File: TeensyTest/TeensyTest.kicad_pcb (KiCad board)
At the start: 2 copper layers, 45 x 34 mm, 31 parts, among them J2 Conn_01x08_Female, J3 Conn_01x03_Female, P1 USB_C_Plug_USB2.0, SW1 SW_Push, SW2 SW_Push, U1 AP2114H, U2 MK20DX256VLH7, U3 MKL02Z32VFG4, Y1 Crystal_GND24

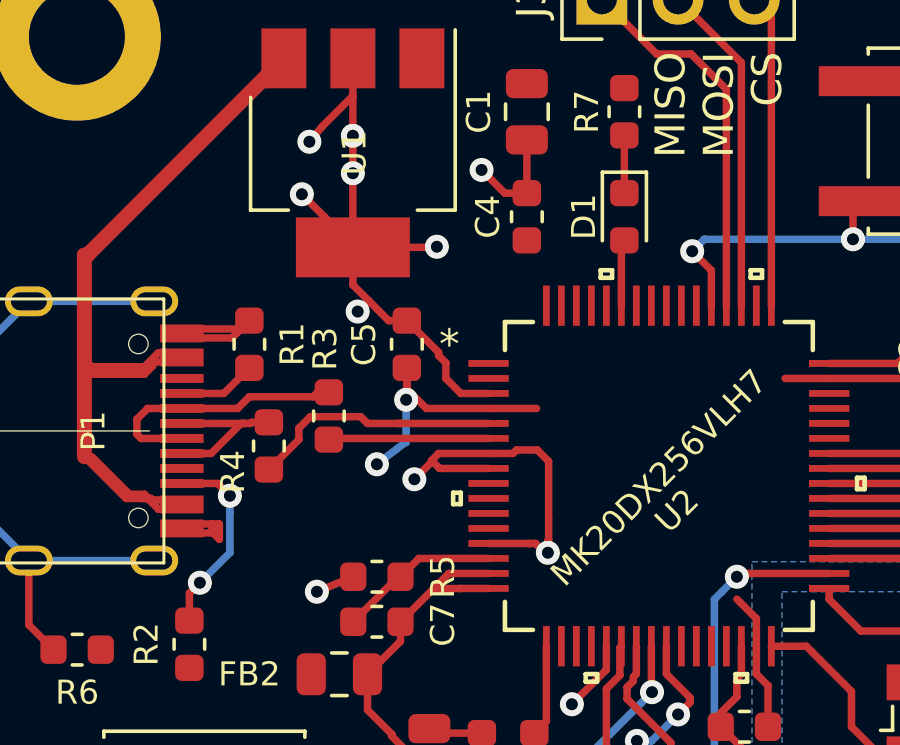
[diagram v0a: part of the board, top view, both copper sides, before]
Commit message: Moved C4 closer to pins 7 & 8
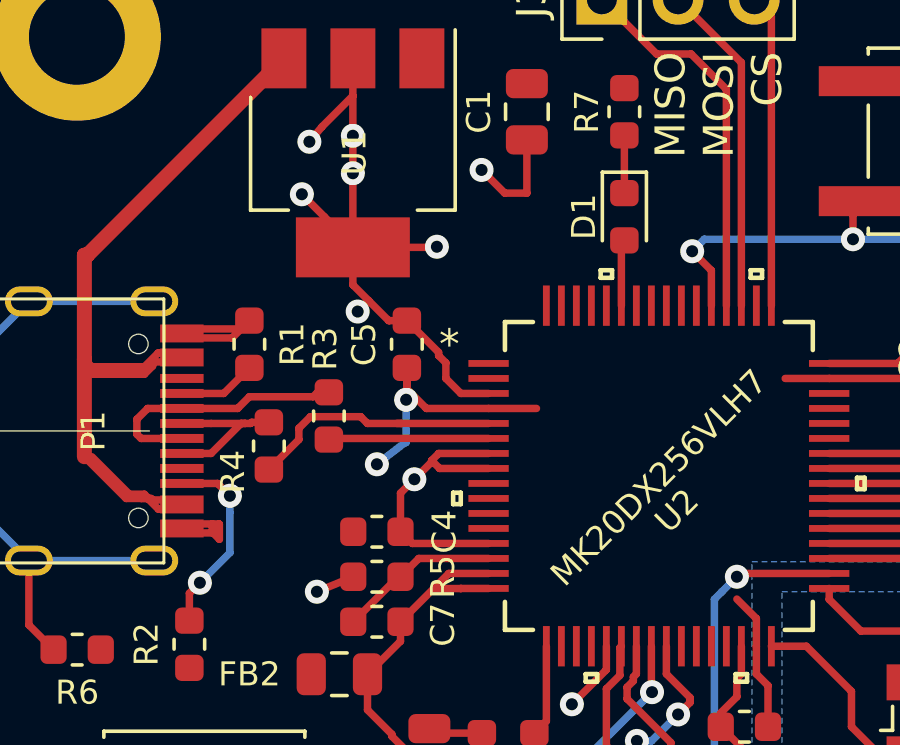
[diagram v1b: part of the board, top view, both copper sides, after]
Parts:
- moved C4 11.6 mm to (29.1, 55.9), turned to 0 degrees
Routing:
- net +3V3: track 61.7 -> 59.4 mm, vias 15 -> 14
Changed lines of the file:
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@@
     (thickness 1.6)
     (drawings 12)
-    (tracks 359)
+    (tracks 349)
     (zones 0)
     (modules 31)
@@
   )
   (module Capacitor_SMD:C_0603_1608Metric (layer F.Cu)
-    (at 34.1 45.36 90)
+    (at 29.1 55.86)
     (descr "Capacitor SMD 0603 (1608 Metric), square (rectangular) end terminal, IPC_7351 nominal, (Body size source: http://www.tortai-tech.com/upload/download/2011102023233369053.pdf), generated with kicad-footprint-generator")
     (tags capacitor)
     (attr smd)
-    (fp_text reference C4 (at 0 -1.3 90) (layer F.SilkS)
-      (effects (font (size 0.8 0.8) (thickness 0.1)))
-    )
-    (fp_text value 0.1uF (at 0 1.43 90) (layer F.Fab)
-      (effects (font (size 0.8 0.8) (thickness 0.1)))
-    )
-    (fp_text user %R (at 0 0 90) (layer F.Fab)
+    (fp_text reference C4 (at 2.25 0 90) (layer F.SilkS)
+      (effects (font (size 0.8 0.8) (thickness 0.1)))
+    )
+    (fp_text value 0.1uF (at 0 1.43) (layer F.Fab)
+      (effects (font (size 0.8 0.8) (thickness 0.1)))
+    )
+    (fp_text user %R (at 0 0) (layer F.Fab)
       (effects (font (size 0.8 0.8) (thickness 0.1)))
     )
@@
     (fp_line (start -0.8 -0.4) (end 0.8 -0.4) (layer F.Fab) (width 0.1))
     (fp_line (start -0.8 0.4) (end -0.8 -0.4) (layer F.Fab) (width 0.1))
-    (pad 2 smd roundrect (at 0.7875 0 90) (size 0.875 0.95) (layers F.Cu F.Paste F.Mask) (roundrect_rratio 0.25)
+    (pad 2 smd roundrect (at 0.7875 0) (size 0.875 0.95) (layers F.Cu F.Paste F.Mask) (roundrect_rratio 0.25)
       (net 1 +3V3))
-    (pad 1 smd roundrect (at -0.7875 0 90) (size 0.875 0.95) (layers F.Cu F.Paste F.Mask) (roundrect_rratio 0.25)
+    (pad 1 smd roundrect (at -0.7875 0) (size 0.875 0.95) (layers F.Cu F.Paste F.Mask) (roundrect_rratio 0.25)
       (net 2 GND))
     (model ${KISYS3DMOD}/Capacitor_SMD.3dshapes/C_0603_1608Metric.wrl
@@
   (segment (start 41.705684 67.139999) (end 41.705684 68.184316) (width 0.25) (layer B.Cu) (net 1))
   (segment (start 41.705684 68.184316) (end 41.22 68.67) (width 0.25) (layer B.Cu) (net 1))
-  (segment (start 33.636984 53.249999) (end 33.751998 53.134985) (width 0.25) (layer F.Cu) (net 1))
-  (segment (start 34.448002 53.134985) (end 34.825002 53.511985) (width 0.25) (layer F.Cu) (net 1))
-  (segment (start 34.825002 53.511985) (end 34.825002 55.458002) (width 0.25) (layer F.Cu) (net 1))
-  (segment (start 33.751998 53.134985) (end 34.448002 53.134985) (width 0.25) (layer F.Cu) (net 1))
-  (segment (start 32.8231 53.249999) (end 33.636984 53.249999) (width 0.25) (layer F.Cu) (net 1))
   (segment (start 28.3125 57.36) (end 27.1 57.86) (width 0.25) (layer F.Cu) (net 1))
   (via (at 27.1 57.86) (size 0.8) (drill 0.4) (layers F.Cu B.Cu) (net 1))
-  (via (at 34.8 56.56) (size 0.8) (drill 0.4) (layers F.Cu B.Cu) (net 1))
-  (segment (start 34.825002 55.458002) (end 34.825002 56.134998) (width 0.25) (layer F.Cu) (net 1))
-  (segment (start 34.8 56.16) (end 34.8 56.56) (width 0.25) (layer F.Cu) (net 1))
-  (segment (start 34.825002 56.134998) (end 34.8 56.16) (width 0.25) (layer F.Cu) (net 1))
-  (segment (start 34.190001 56.250001) (end 34.2 56.26) (width 0.25) (layer F.Cu) (net 1))
-  (segment (start 32.8231 56.250001) (end 34.190001 56.250001) (width 0.25) (layer F.Cu) (net 1))
-  (segment (start 34.190001 56.250001) (end 34.390001 56.250001) (width 0.25) (layer F.Cu) (net 1))
-  (segment (start 34.7 56.56) (end 34.8 56.56) (width 0.25) (layer F.Cu) (net 1))
-  (segment (start 34.390001 56.250001) (end 34.7 56.56) (width 0.25) (layer F.Cu) (net 1))
   (segment (start 32.8231 53.75) (end 31.19 53.75) (width 0.25) (layer F.Cu) (net 1))
   (segment (start 31.19 53.75) (end 30.925 53.485) (width 0.25) (layer F.Cu) (net 1))
@@
   (segment (start 30.925 53.535) (end 30.35 54.11) (width 0.25) (layer F.Cu) (net 1))
   (segment (start 30.925 53.485) (end 30.925 53.535) (width 0.25) (layer F.Cu) (net 1))
+  (segment (start 29.8875 54.5725) (end 30.35 54.11) (width 0.25) (layer F.Cu) (net 1))
+  (segment (start 29.8875 55.86) (end 29.8875 54.5725) (width 0.25) (layer F.Cu) (net 1))
+  (segment (start 30.277501 56.250001) (end 29.8875 55.86) (width 0.25) (layer F.Cu) (net 1))
+  (segment (start 32.8231 56.250001) (end 30.277501 56.250001) (width 0.25) (layer F.Cu) (net 1))
   (segment (start 24.5725 49.1) (end 24.85 48.8225) (width 0.25) (layer F.Cu) (net 2))
   (segment (start 22.6 49.1) (end 24.5725 49.1) (width 0.25) (layer F.Cu) (net 2))

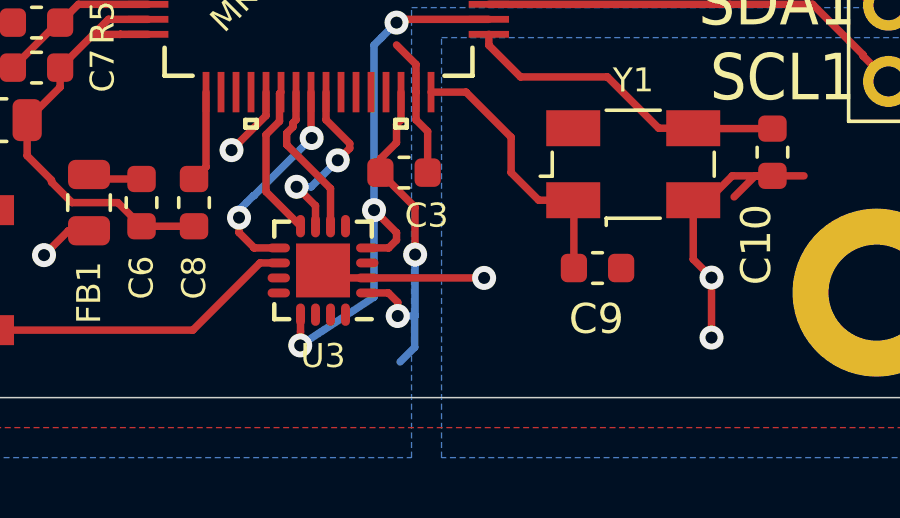
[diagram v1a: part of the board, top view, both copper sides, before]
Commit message: Added extra 100nF cap for MKL02
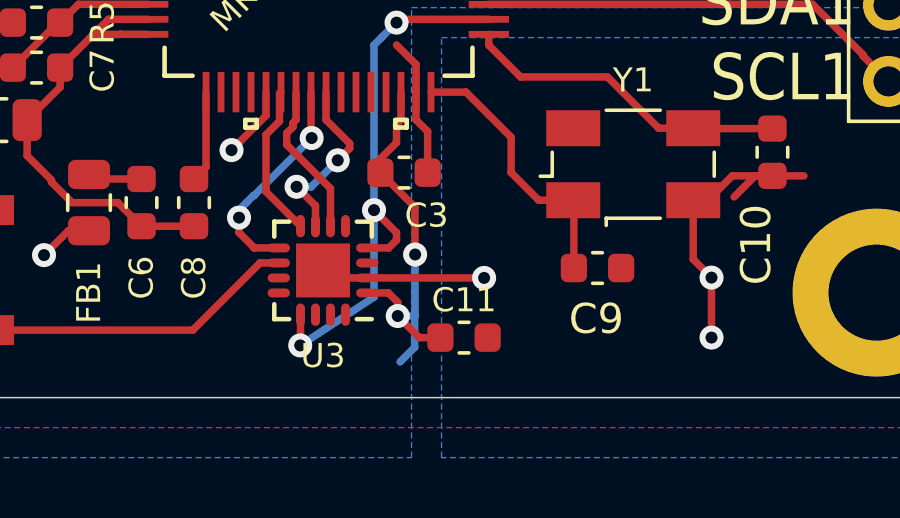
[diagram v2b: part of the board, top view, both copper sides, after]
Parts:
- added C11: 0.1uF, Capacitor_SMD:C_0603_1608Metric, F.Cu at (43.4, 67.9)
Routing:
- net +3V3: track 59.4 -> 61.1 mm
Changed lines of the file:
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@@
     (thickness 1.6)
     (drawings 12)
-    (tracks 349)
+    (tracks 351)
     (zones 0)
-    (modules 31)
+    (modules 32)
     (nets 37)
   )
@@
     (add_net "Net-(C9-Pad1)")
     (add_net "Net-(D1-Pad1)")
+    (add_net "Net-(P1-PadA8)")
+    (add_net "Net-(P1-PadB8)")
     (add_net "Net-(P1-PadS1)")
     (add_net "Net-(SW2-Pad1)")
+    (add_net "Net-(U2-Pad1)")
+    (add_net "Net-(U2-Pad10)")
+    (add_net "Net-(U2-Pad11)")
+    (add_net "Net-(U2-Pad12)")
+    (add_net "Net-(U2-Pad18)")
+    (add_net "Net-(U2-Pad19)")
+    (add_net "Net-(U2-Pad2)")
+    (add_net "Net-(U2-Pad20)")
     (add_net "Net-(U2-Pad22)")
     (add_net "Net-(U2-Pad23)")
     (add_net "Net-(U2-Pad24)")
     (add_net "Net-(U2-Pad25)")
+    (add_net "Net-(U2-Pad26)")
+    (add_net "Net-(U2-Pad27)")
+    (add_net "Net-(U2-Pad28)")
+    (add_net "Net-(U2-Pad29)")
+    (add_net "Net-(U2-Pad43)")
+    (add_net "Net-(U2-Pad44)")
+    (add_net "Net-(U2-Pad45)")
+    (add_net "Net-(U2-Pad46)")
+    (add_net "Net-(U2-Pad50)")
+    (add_net "Net-(U2-Pad54)")
+    (add_net "Net-(U2-Pad55)")
+    (add_net "Net-(U2-Pad56)")
+    (add_net "Net-(U2-Pad57)")
+    (add_net "Net-(U2-Pad58)")
+    (add_net "Net-(U2-Pad60)")
+    (add_net "Net-(U2-Pad61)")
+    (add_net "Net-(U2-Pad62)")
+    (add_net "Net-(U2-Pad63)")
+    (add_net "Net-(U2-Pad64)")
+    (add_net "Net-(U2-Pad9)")
+    (add_net "Net-(U3-Pad11)")
+    (add_net "Net-(U3-Pad12)")
+    (add_net "Net-(U3-Pad14)")
+    (add_net "Net-(U3-Pad15)")
+    (add_net "Net-(U3-Pad16)")
+    (add_net "Net-(U3-Pad3)")
+    (add_net "Net-(U3-Pad5)")
     (add_net RESET_B)
     (add_net VBUS)
+  )
+  (module Capacitor_SMD:C_0603_1608Metric (layer F.Cu)
+    (at 43.35 67.86 180)
+    (descr "Capacitor SMD 0603 (1608 Metric), square (rectangular) end terminal, IPC_7351 nominal, (Body size source: http://www.tortai-tech.com/upload/download/2011102023233369053.pdf), generated with kicad-footprint-generator")
+    (tags capacitor)
+    (attr smd)
+    (fp_text reference C11 (at 0 1.25) (layer F.SilkS)
+      (effects (font (size 0.8 0.8) (thickness 0.1)))
+    )
+    (fp_text value 0.1uF (at 0 1.43) (layer F.Fab)
+      (effects (font (size 1 1) (thickness 0.15)))
+    )
+    (fp_text user %R (at 0 0) (layer F.Fab)
+      (effects (font (size 0.4 0.4) (thickness 0.06)))
+    )
+    (fp_line (start 1.48 0.73) (end -1.48 0.73) (layer F.CrtYd) (width 0.05))
+    (fp_line (start 1.48 -0.73) (end 1.48 0.73) (layer F.CrtYd) (width 0.05))
+    (fp_line (start -1.48 -0.73) (end 1.48 -0.73) (layer F.CrtYd) (width 0.05))
+    (fp_line (start -1.48 0.73) (end -1.48 -0.73) (layer F.CrtYd) (width 0.05))
+    (fp_line (start -0.162779 0.51) (end 0.162779 0.51) (layer F.SilkS) (width 0.12))
+    (fp_line (start -0.162779 -0.51) (end 0.162779 -0.51) (layer F.SilkS) (width 0.12))
+    (fp_line (start 0.8 0.4) (end -0.8 0.4) (layer F.Fab) (width 0.1))
+    (fp_line (start 0.8 -0.4) (end 0.8 0.4) (layer F.Fab) (width 0.1))
+    (fp_line (start -0.8 -0.4) (end 0.8 -0.4) (layer F.Fab) (width 0.1))
+    (fp_line (start -0.8 0.4) (end -0.8 -0.4) (layer F.Fab) (width 0.1))
+    (pad 2 smd roundrect (at 0.7875 0 180) (size 0.875 0.95) (layers F.Cu F.Paste F.Mask) (roundrect_rratio 0.25)
+      (net 1 +3V3))
+    (pad 1 smd roundrect (at -0.7875 0 180) (size 0.875 0.95) (layers F.Cu F.Paste F.Mask) (roundrect_rratio 0.25)
+      (net 2 GND))
+    (model ${KISYS3DMOD}/Capacitor_SMD.3dshapes/C_0603_1608Metric.wrl
+      (at (xyz 0 0 0))
+      (scale (xyz 1 1 1))
+      (rotate (xyz 0 0 0))
+    )
   )
   (module USB-C-Power-tester:TYPE-C-31-M-12 (layer F.Cu)
@@
   (segment (start 30.277501 56.250001) (end 29.8875 55.86) (width 0.25) (layer F.Cu) (net 1))
   (segment (start 32.8231 56.250001) (end 30.277501 56.250001) (width 0.25) (layer F.Cu) (net 1))
+  (segment (start 41.139999 67.139999) (end 41.86 67.86) (width 0.25) (layer F.Cu) (net 1))
+  (segment (start 41.86 67.86) (end 42.5625 67.86) (width 0.25) (layer F.Cu) (net 1))
   (segment (start 24.5725 49.1) (end 24.85 48.8225) (width 0.25) (layer F.Cu) (net 2))
   (segment (start 22.6 49.1) (end 24.5725 49.1) (width 0.25) (layer F.Cu) (net 2))

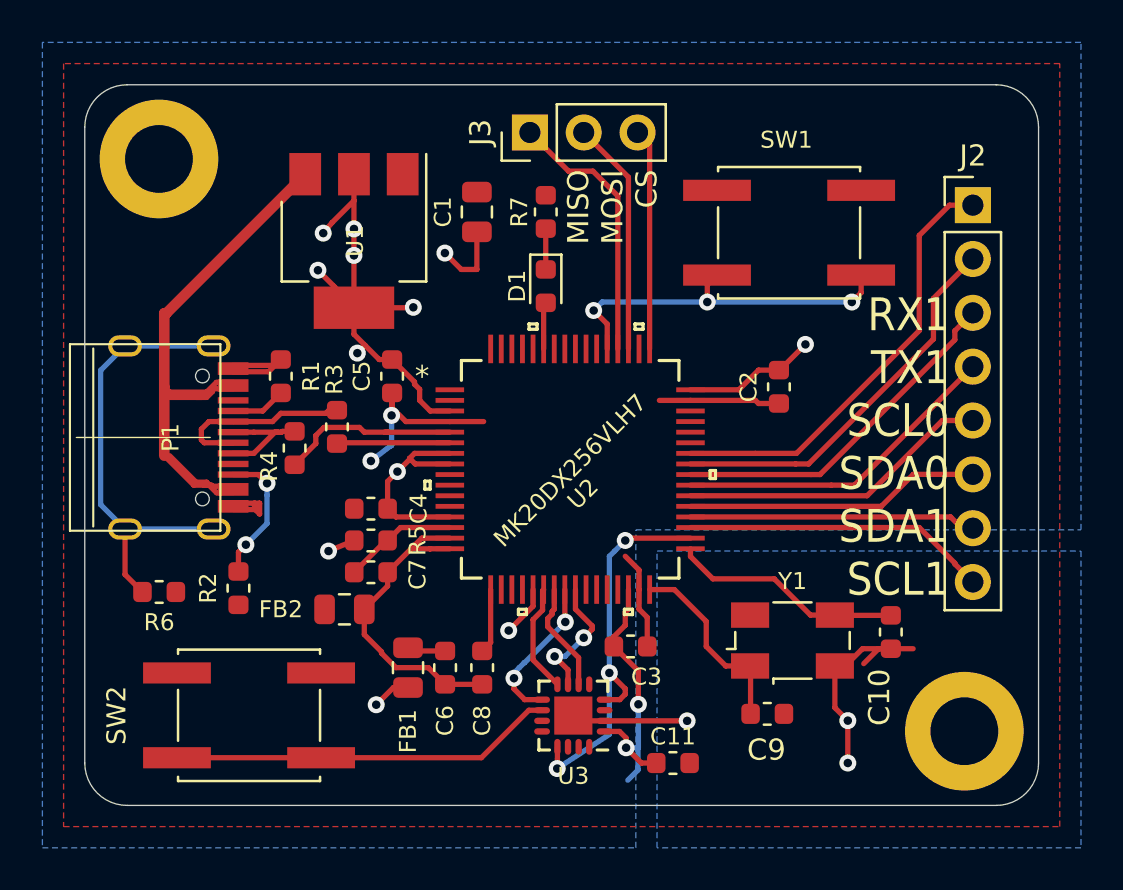
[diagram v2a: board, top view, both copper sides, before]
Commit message: added Teensy3.2 schematic as reference, added CLK pin for SPI comms
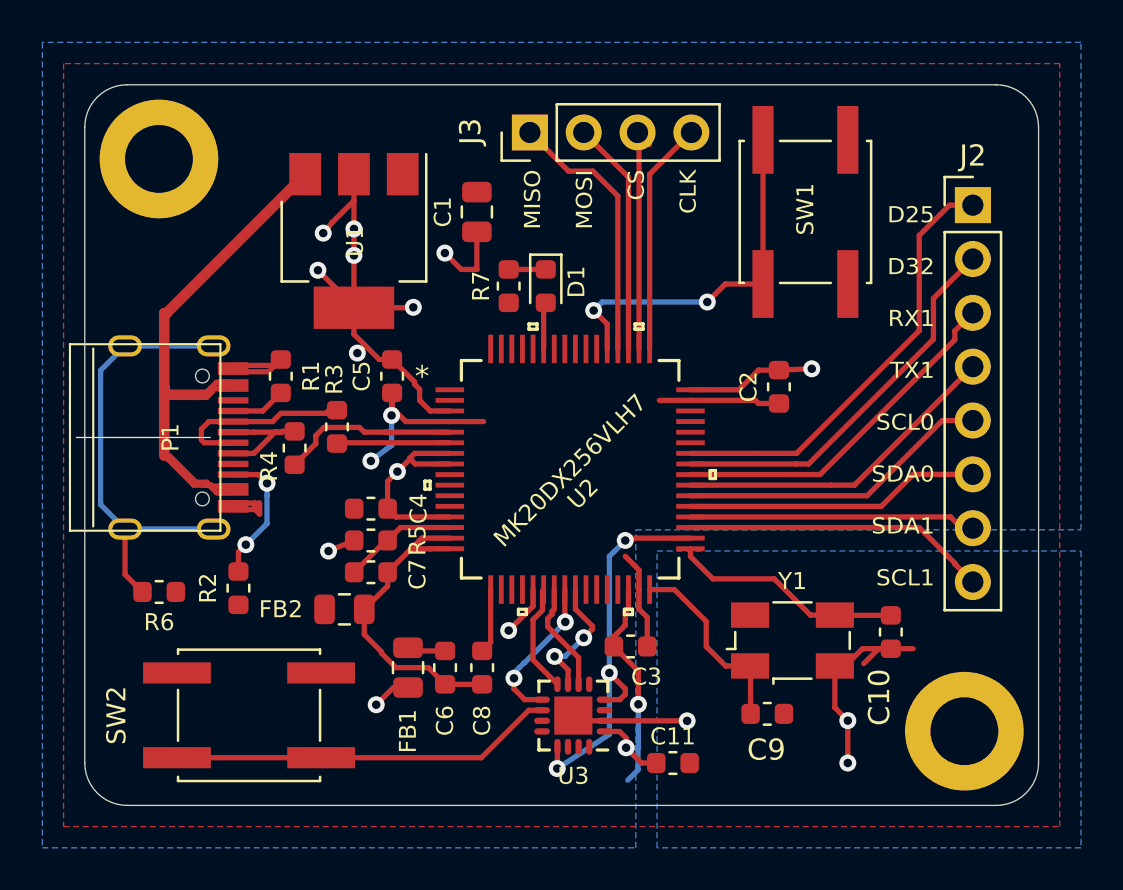
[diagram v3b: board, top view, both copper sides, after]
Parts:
- J3: value Conn_01x03_Female -> Conn_01x04_Female; footprint Connector_PinHeader_2.54mm:PinHeader_1x03_P2.54mm_Vertical -> Connector_PinHeader_2.54mm:PinHeader_1x04_P2.54mm_Vertical
- moved R7 3.91 mm to (35.6, 45.4), turned to 270 degrees
- moved SW1 1.25 mm to (49.6, 41.9), turned to 90 degrees
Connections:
- J3 pad 3: /D10 -> /D13
- U2 pad 50: (no net) -> /D13
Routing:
- net /D13: track 0.00 -> 11.0 mm
- net /D10: track 10.4 -> 11.0 mm
- net /D28: track 17.3 -> 17.4 mm, vias 3 -> 2
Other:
- board text added: "D25 D32 RX1 TX1 SCL0 SDA0 SDA1 SCL1"
- board text added: "MISO MOSI CS CLK"
- board text removed: "MISO MOSI CS"
- board text removed: "RX1 TX1 SCL0 SDA0 SDA1 SCL1"
